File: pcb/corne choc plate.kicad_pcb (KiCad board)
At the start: 2 copper layers, 136.2 x 88.4 mm, 27 parts, among them SW1 SW_PUSH, SW10 SW_PUSH, SW11 SW_PUSH, SW12 SW_PUSH, SW13 SW_PUSH, SW14 SW_PUSH, SW15 SW_PUSH, SW16 SW_PUSH, SW17 SW_PUSH, SW18 SW_PUSH, SW19 SW_PUSH, SW2 SW_PUSH, SW20 SW_PUSH, SW3 SW_PUSH, SW4 SW_PUSH, SW45 SW_PUSH, SW46 SW_PUSH, SW5 SW_PUSH, SW6 SW_PUSH, SW7 SW_PUSH, SW8 SW_PUSH, SW9 SW_PUSH

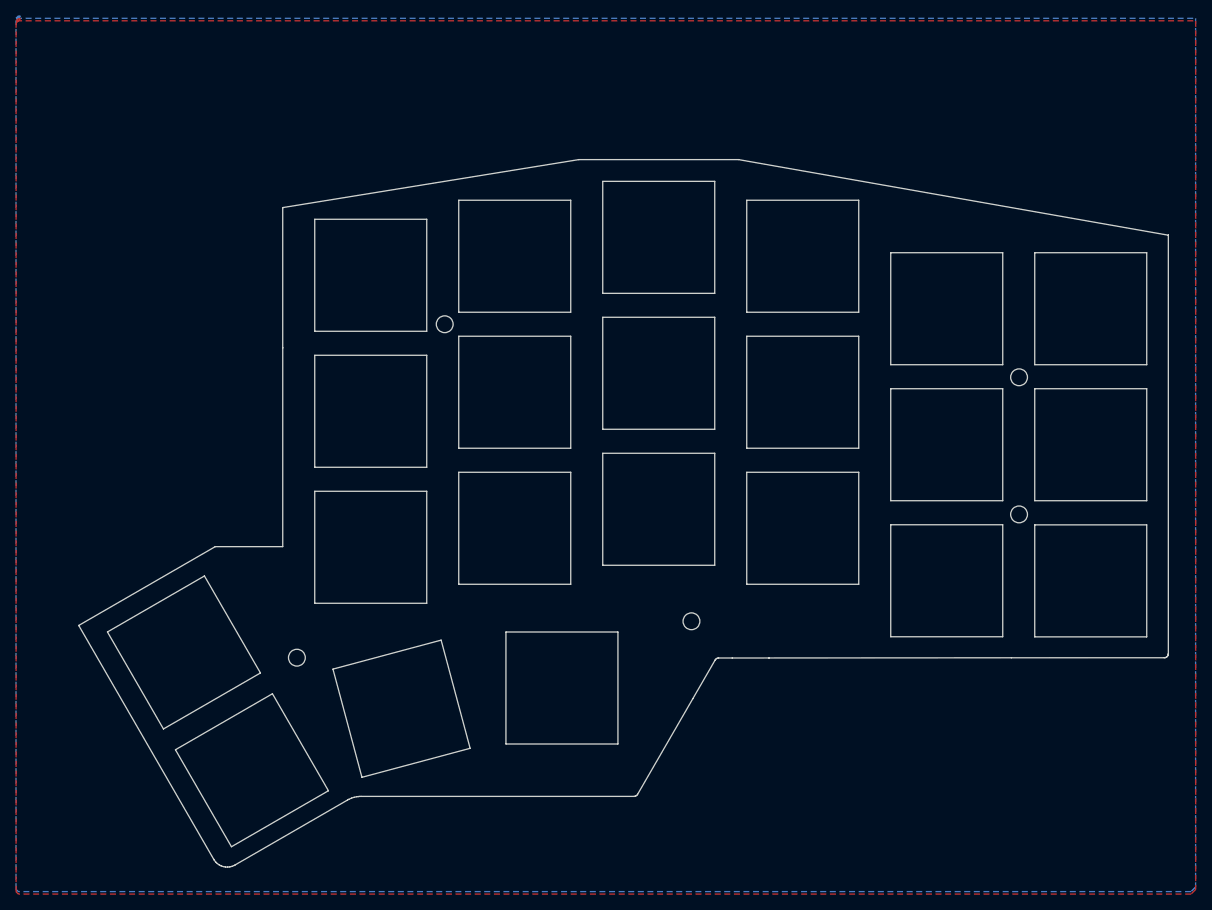
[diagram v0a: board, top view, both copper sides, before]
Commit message: v2.1: 1.15 mm key-to-edge gap, matching switch orientation, LED moves
- Keycaps sit 1.15 mm from the edge wherever it follows them; outer side
  edges move out, and every hot-swap socket pad clears the edge by 0.33 mm.
- The left inner thumb keys no longer turn 180 degrees: every switch, and
  every per-key LED, faces the same way.
- Underglow LED32 and its left twin LED5 move, mirrored, clear of the
  trackpoint driver's hand-soldered pads.
- Mounting holes for the unused OLED cover removed (tools/strip.py).
- Plates follow the moved outer edges; renders show both plates fitted.
- Build: finish pass runs until no dangling copper is left.
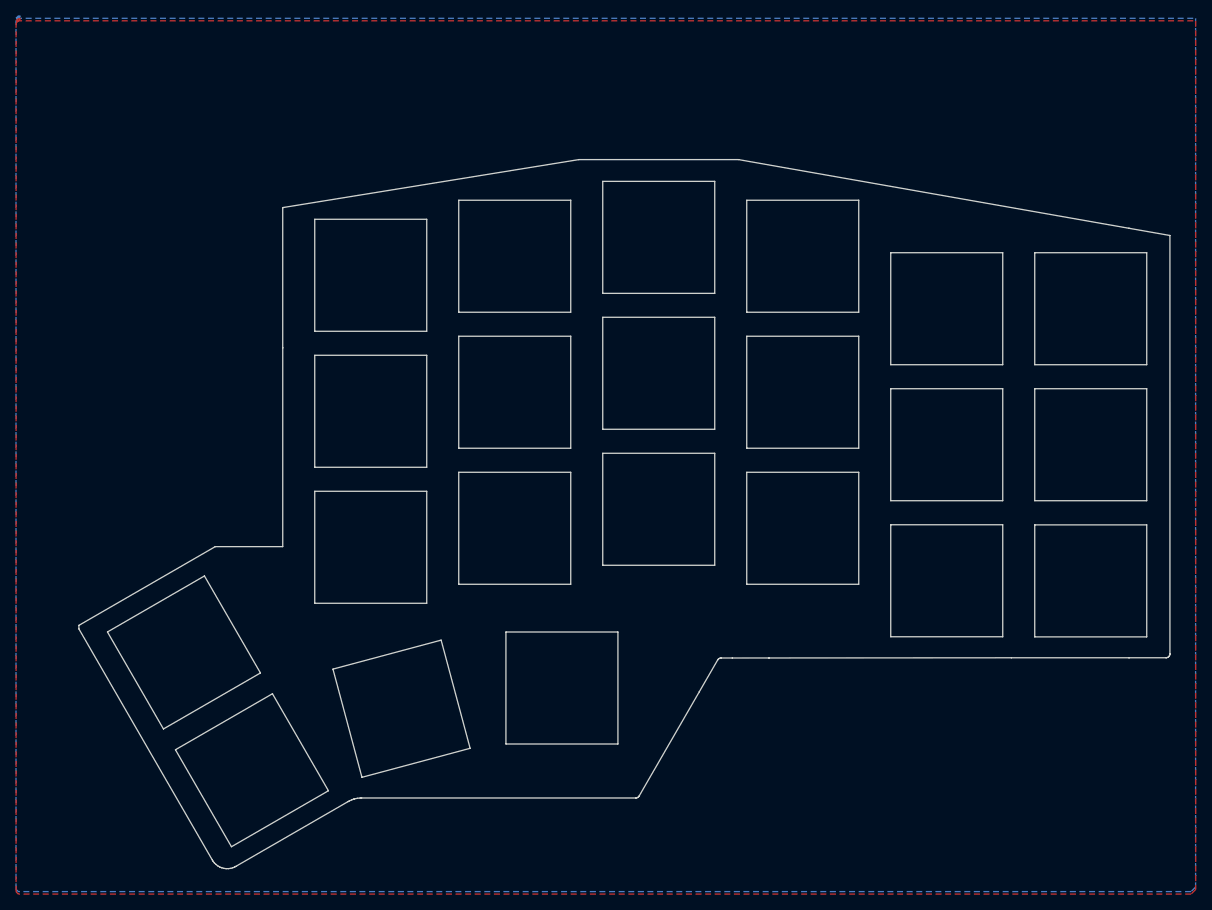
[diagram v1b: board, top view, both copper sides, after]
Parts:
- removed ?: M2_HOLE_NPH, holykeebs:M2_HOLE_NPH
- removed h2 (x4): h2, holykeebs:M2_HOLE_NPH
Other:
- board size 136.2 x 88.4 mm -> 136.4 x 88.6 mm

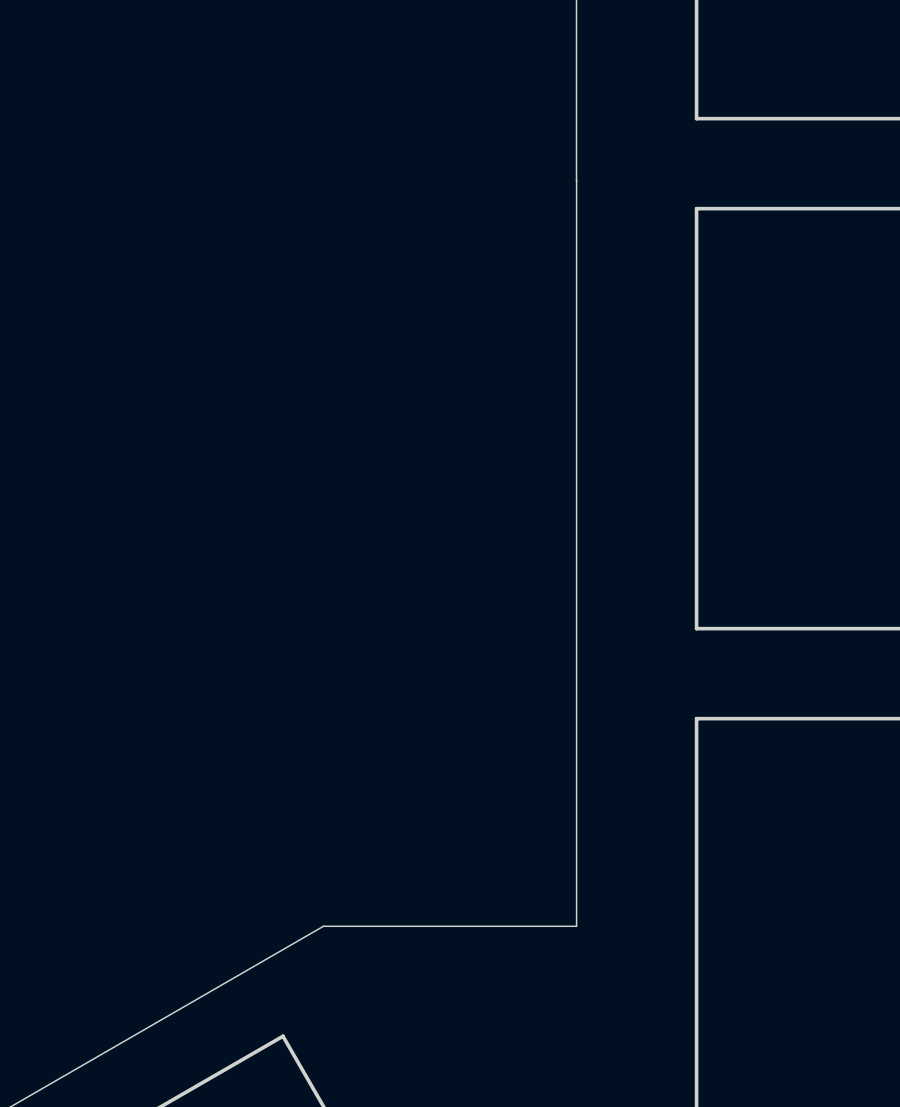
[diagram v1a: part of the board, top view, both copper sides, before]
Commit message: v2.1: driver pads per drawing, diagonal plate edge, no-OLED renders
- Trackpoint driver host pads follow Sprintek's drawing: 1.0 mm wide at
  1.80 mm pitch, leaving 0.8 mm between them for hand soldering.
- The switch plate carries the upper inner thumb key's top edge straight
  on to its inner edge (2.6 mm clear of the OLED header) instead of a step.
- Render script gains assembled top-down and no-OLED views.
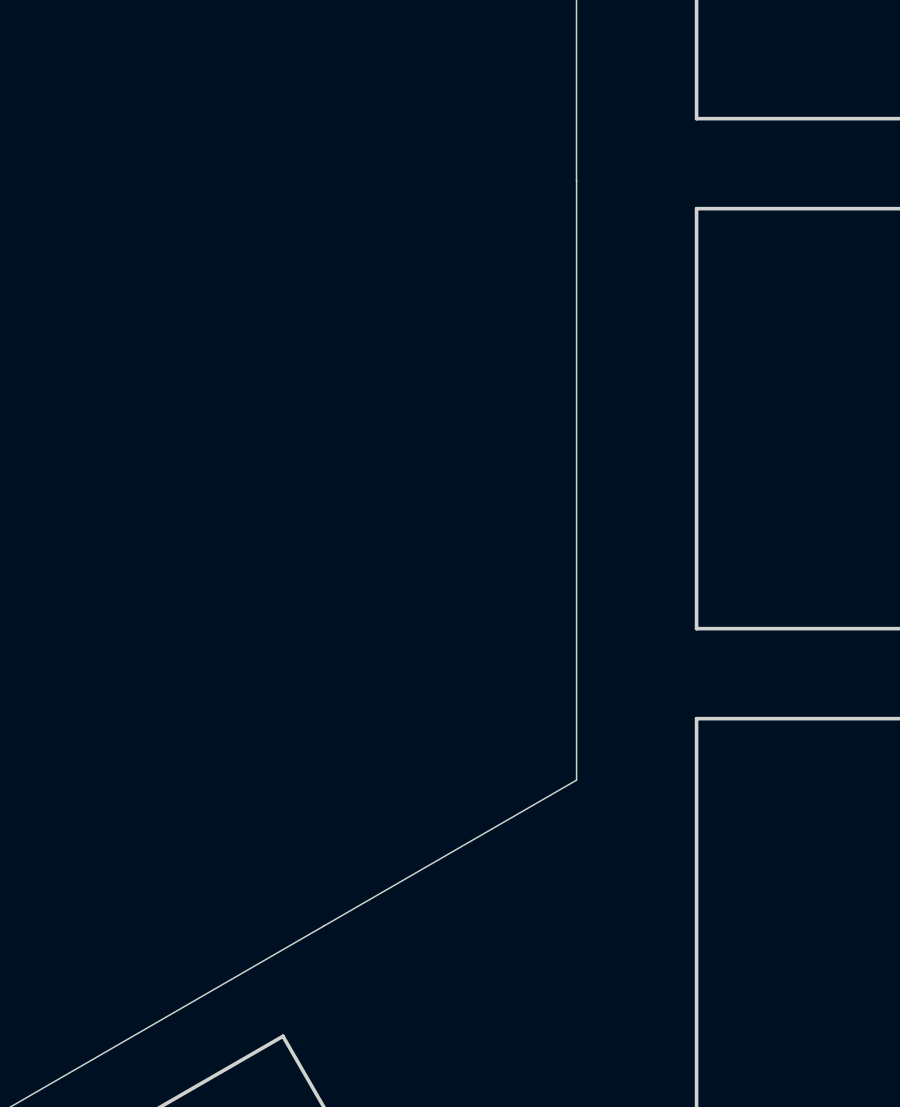
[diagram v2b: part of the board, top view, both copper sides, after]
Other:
- outline, holes or cut-outs redrawn

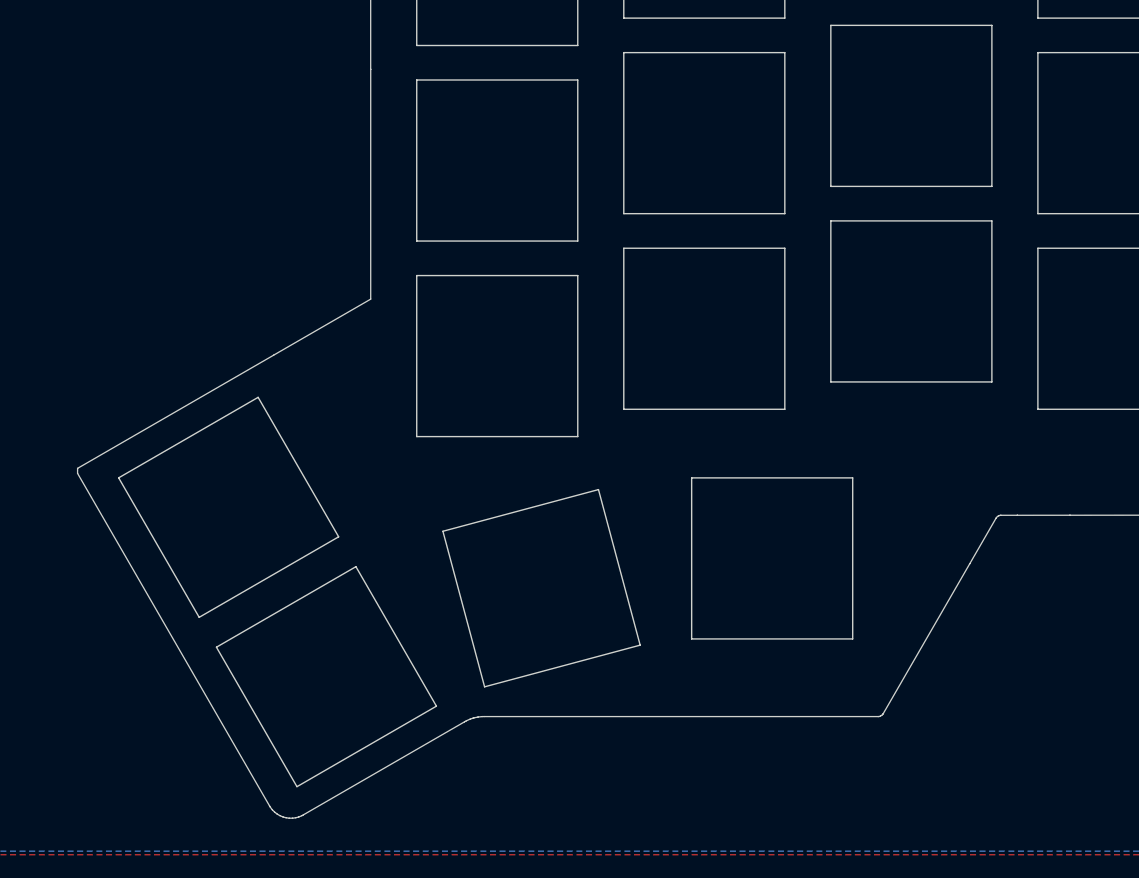
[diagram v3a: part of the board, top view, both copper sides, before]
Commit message: Thumb cluster on the index-aligned arc, wider inner edge, 15-degree marks
- The thumb cluster sits 1.37 mm further in and 0.98 mm higher, so the middle
  thumb key meets the bottom index key the way it meets the inner key (same
  corner gap, opening at 15 degrees); the trackpoint moves with it.
- The inner straight edge moves out by what the upper inner thumb key needs
  to keep the 1.15 mm gap (6.92 mm in all); jacks stay centred in the strip,
  1.24 mm from the controller pins.
- Silkscreen protractor marks ("15°") in the three thumb gaps, on the PCB
  front and both faces of every switch plate.
- Both variants rebuilt; plate renders include silkscreen.
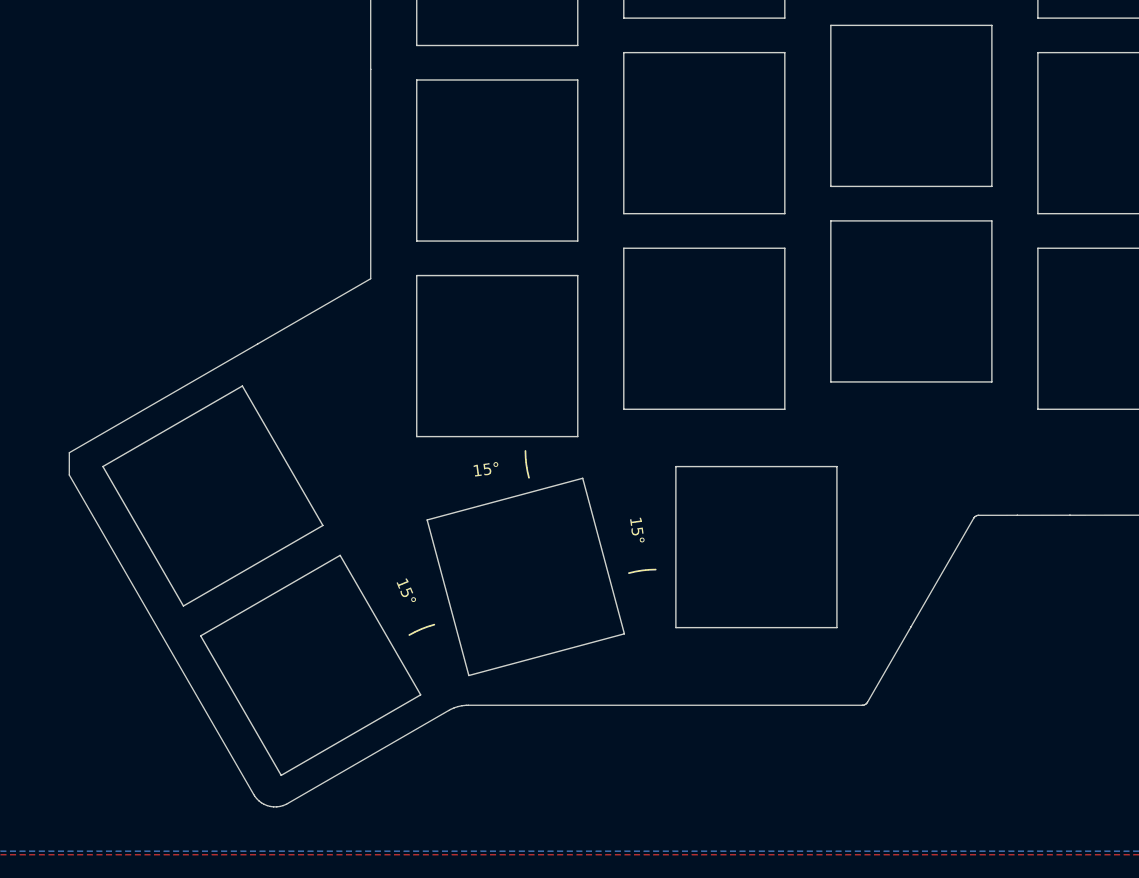
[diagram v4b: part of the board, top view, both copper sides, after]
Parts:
- moved SW19 1.69 mm to (201.3, 116.5)
- moved SW20 1.69 mm to (181.3, 119.1)
- moved SW45 1.69 mm to (162.6, 126.8)
- moved SW46 1.69 mm to (154.1, 112.1)
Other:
- board size 136.4 x 88.6 mm -> 137.1 x 87.6 mm
- board text added: "15°"
